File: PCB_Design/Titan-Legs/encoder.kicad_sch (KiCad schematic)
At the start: 1 part

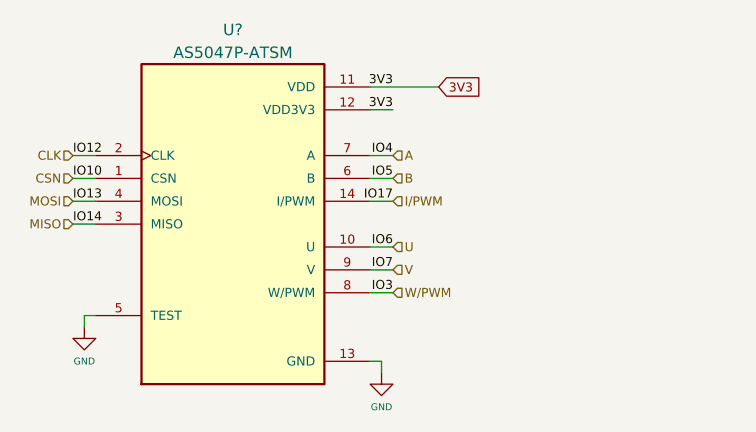
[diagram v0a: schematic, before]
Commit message: schematics 1st iteration completed
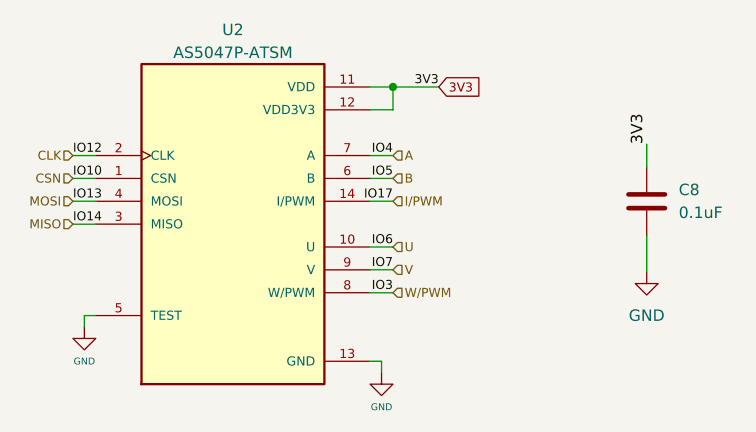
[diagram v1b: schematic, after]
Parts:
- added C8: 0.1uF, symbol Device:C
- gave numbers to parts that had none: 1
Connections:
- net 3V3: now also C8.1
- net GND: now also C8.2
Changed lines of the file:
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@@
 (kicad_sch (version 20211123) (generator eeschema)
   (paper "A4")
+  (junction (at 139.7 77.47) (diameter 0) (color 0 0 0 0)
+  )
   (wire (pts (xy 105.41 102.87) (xy 105.41 104.14))
     (stroke (width 0) (type default) (color 0 0 0 0))
@@
     (stroke (width 0) (type default) (color 0 0 0 0))
   )
+  (wire (pts (xy 139.7 77.47) (xy 144.78 77.47))
+    (stroke (width 0) (type default) (color 0 0 0 0))
+  )
   (wire (pts (xy 104.14 90.17) (xy 106.68 90.17))
     (stroke (width 0) (type default) (color 0 0 0 0))
@@
     (stroke (width 0) (type default) (color 0 0 0 0))
   )
+  (wire (pts (xy 137.16 77.47) (xy 139.7 77.47))
+    (stroke (width 0) (type default) (color 0 0 0 0))
+  )
   (wire (pts (xy 106.68 102.87) (xy 105.41 102.87))
     (stroke (width 0) (type default) (color 0 0 0 0))
   )
+  (wire (pts (xy 139.7 77.47) (xy 139.7 80.01))
+    (stroke (width 0) (type default) (color 0 0 0 0))
+  )
+  (wire (pts (xy 167.894 93.98) (xy 167.894 98.044))
+    (stroke (width 0) (type default) (color 0 0 0 0))
+  )
   (wire (pts (xy 104.14 85.09) (xy 106.68 85.09))
     (stroke (width 0) (type default) (color 0 0 0 0))
@@
     (stroke (width 0) (type default) (color 0 0 0 0))
   )
-  (wire (pts (xy 137.16 77.47) (xy 144.78 77.47))
-    (stroke (width 0) (type default) (color 0 0 0 0))
-  )
   (wire (pts (xy 104.14 92.71) (xy 106.68 92.71))
     (stroke (width 0) (type default) (color 0 0 0 0))
@@
     (stroke (width 0) (type default) (color 0 0 0 0))
   )
+  (wire (pts (xy 167.894 83.82) (xy 167.894 86.36))
+    (stroke (width 0) (type default) (color 0 0 0 0))
+  )
   (wire (pts (xy 138.43 107.95) (xy 138.43 109.22))
     (stroke (width 0) (type default) (color 0 0 0 0))
@@
     (stroke (width 0) (type default) (color 0 0 0 0))
   )
-  (label "3V3" (at 139.7 77.47 180)
+  (label "3V3" (at 144.78 77.47 180)
     (effects (font (size 1 1)) (justify right bottom))
   )
@@
     (effects (font (size 1 1)) (justify right bottom))
   )
+  (label "3V3" (at 167.894 83.82 90)
+    (effects (font (size 1.27 1.27)) (justify left bottom))
+  )
   (label "IO14" (at 104.14 92.71 0)
     (effects (font (size 1 1)) (justify left bottom))
@@
   (label "IO10" (at 104.14 87.63 0)
     (effects (font (size 1 1)) (justify left bottom))
-  )
-  (label "3V3" (at 139.7 80.01 180)
-    (effects (font (size 1 1)) (justify right bottom))
   )
   (label "IO13" (at 104.14 90.17 0)
@@
   (symbol (lib_id "AS5047P-ATSM:AS5047P-ATSM") (at 121.92 92.71 0) (unit 1)
     (in_bom yes) (on_board yes)
-    (property "Reference" "U?" (id 0) (at 121.92 71.12 0))
+    (property "Reference" "U2" (id 0) (at 121.92 71.12 0))
     (property "Value" "AS5047P-ATSM" (id 1) (at 121.92 73.66 0))
     (property "Footprint" "SOP65P640X120-14N" (id 2) (at 121.92 92.71 0)
@@
     (pin "9")
   )
+  (symbol (lib_id "Device:C") (at 167.894 90.17 0) (unit 1)
+    (in_bom yes) (on_board yes) (fields_autoplaced)
+    (property "Reference" "C8" (id 0) (at 171.45 88.8999 0)
+      (effects (font (size 1.27 1.27)) (justify left))
+    )
+    (property "Value" "0.1uF" (id 1) (at 171.45 91.4399 0)
+      (effects (font (size 1.27 1.27)) (justify left))
+    )
+    (property "Footprint" "" (id 2) (at 168.8592 93.98 0)
+      (effects (font (size 1.27 1.27)) hide)
+    )
+    (property "Datasheet" "~" (id 3) (at 167.894 90.17 0)
+      (effects (font (size 1.27 1.27)) hide)
+    )
+    (pin "1")
+    (pin "2")
+  )
   (symbol (lib_id "power:GND") (at 138.43 109.22 0) (unit 1)
     (in_bom yes) (on_board yes)
-    (property "Reference" "#PWR?" (id 0) (at 138.43 115.57 0)
+    (property "Reference" "#PWR021" (id 0) (at 138.43 115.57 0)
       (effects (font (size 1.27 1.27)) hide)
     )
@@
   (symbol (lib_id "power:GND") (at 105.41 104.14 0) (unit 1)
     (in_bom yes) (on_board yes)
-    (property "Reference" "#PWR?" (id 0) (at 105.41 110.49 0)
+    (property "Reference" "#PWR020" (id 0) (at 105.41 110.49 0)
       (effects (font (size 1.27 1.27)) hide)
     )
@@
       (effects (font (size 1.27 1.27)) hide)
     )
+    (pin "1")
+  )
+  (symbol (lib_name "GND_1") (lib_id "power:GND") (at 167.894 98.044 0) (unit 1)
+    (in_bom yes) (on_board yes) (fields_autoplaced)
+    (property "Reference" "#PWR022" (id 0) (at 167.894 104.394 0)
+      (effects (font (size 1.27 1.27)) hide)
+    )
+    (property "Value" "GND" (id 1) (at 167.894 102.87 0))
+    (property "Footprint" "" (id 2) (at 167.894 98.044 0)
+      (effects (font (size 1.27 1.27)) hide)
+    )
+    (property "Datasheet" "" (id 3) (at 167.894 98.044 0)
+      (effects (font (size 1.27 1.27)) hide)
+    )

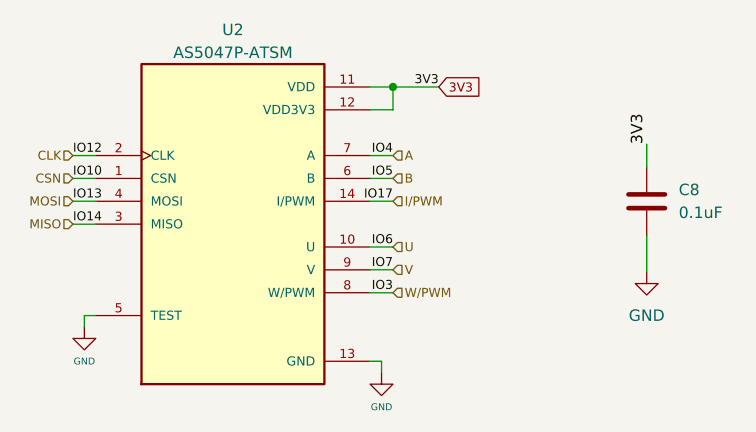
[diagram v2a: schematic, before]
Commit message: Added AMS1117 for ESP32-S3
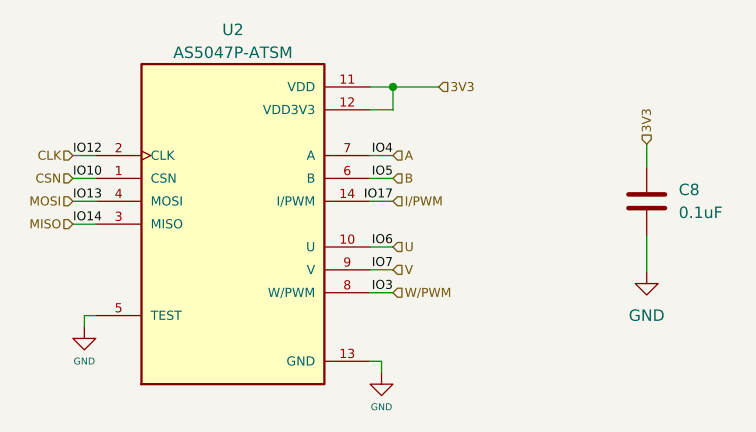
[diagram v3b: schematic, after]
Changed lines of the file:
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@@
     (stroke (width 0) (type default) (color 0 0 0 0))
-  )
-  (label "3V3" (at 144.78 77.47 180)
-    (effects (font (size 1 1)) (justify right bottom))
   )
   (label "IO12" (at 104.14 85.09 0)
@@
   (label "IO5" (at 139.7 87.63 180)
     (effects (font (size 1 1)) (justify right bottom))
-  )
-  (label "3V3" (at 167.894 83.82 90)
-    (effects (font (size 1.27 1.27)) (justify left bottom))
   )
   (label "IO14" (at 104.14 92.71 0)
@@
     (effects (font (size 1 1)) (justify right bottom))
   )
-  (global_label "3V3" (shape input) (at 144.78 77.47 0) (fields_autoplaced)
-    (effects (font (size 1 1)) (justify left))
-    (property "Intersheet References" "${INTERSHEET_REFS}" (id 0) (at 149.4419 77.4075 0)
-      (effects (font (size 1 1)) (justify left) hide)
-    )
-  )
   (hierarchical_label "V" (shape input) (at 139.7 97.79 0)
     (effects (font (size 1 1)) (justify left))
@@
     (effects (font (size 1 1)) (justify right))
   )
+  (hierarchical_label "3V3" (shape input) (at 167.894 83.82 90)
+    (effects (font (size 1 1)) (justify left))
+  )
   (hierarchical_label "A" (shape input) (at 139.7 85.09 0)
     (effects (font (size 1 1)) (justify left))
@@
     (effects (font (size 1 1)) (justify left))
   )
+  (hierarchical_label "3V3" (shape input) (at 144.78 77.47 0)
+    (effects (font (size 1 1)) (justify left))
+  )

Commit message: added electrolytic capacitors
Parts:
- C8: footprint (none) -> Capacitor_SMD:C_0603_1608Metric
- U2: footprint SOP65P640X120-14N -> ENCODER:SOP65P640X120-14N
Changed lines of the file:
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@@
     (property "Reference" "U2" (id 0) (at 121.92 71.12 0))
     (property "Value" "AS5047P-ATSM" (id 1) (at 121.92 73.66 0))
-    (property "Footprint" "SOP65P640X120-14N" (id 2) (at 121.92 92.71 0)
+    (property "Footprint" "ENCODER:SOP65P640X120-14N" (id 2) (at 121.92 92.71 0)
       (effects (font (size 1.27 1.27)) (justify bottom) hide)
     )
@@
       (effects (font (size 1.27 1.27)) (justify left))
     )
-    (property "Footprint" "" (id 2) (at 168.8592 93.98 0)
+    (property "Footprint" "Capacitor_SMD:C_0603_1608Metric" (id 2) (at 168.8592 93.98 0)
       (effects (font (size 1.27 1.27)) hide)
     )
